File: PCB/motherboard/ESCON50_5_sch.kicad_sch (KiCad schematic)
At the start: 0 parts

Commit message: aggiunto driver escon in libreria e nel progetto schematico
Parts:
- added E1: escon, ESCON:escon_vero, symbol escon50_5:ESCON_50/5
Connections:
- new net +24V: E1.7 (Vcc), E1.8 (Vcc)
- new net +5V: E1.11 (+5_VDC)
- new net GND: E1.10 (GND), E1.23 (GND), E1.9 (GND)
- new net MW1: E1.1 (motor_winding_1), E1.2 (motor_winding_1)
- new net MW2: E1.3 (motor_winding_2), E1.4 (motor_winding_2)
- new net MW3: E1.5 (motor_winding_3), E1.6 (motor_winding_3)

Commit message: test kicad collab
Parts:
- added C14, C16: 150p, Capacitor_SMD:C_1206_3216Metric_Pad1.33x1.80mm_HandSolder, symbol Device:C
- added C15, C17: 330p, Capacitor_SMD:C_1206_3216Metric_Pad1.33x1.80mm_HandSolder, symbol Device:C
- added L2, L3: 22uH, induttorejlpcb_escon:Senza-titolo, symbol PA5433_223NLT:PA5433.223NLT
- added R11, R12: 390, Resistor_SMD:R_1206_3216Metric_Pad1.30x1.75mm_HandSolder, symbol Device:R
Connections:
- net GND: now also C14.2, C16.2, R11.2, R12.2
- net MW2: now also L3.1
- net MW3: now also L2.1
- new net: C15.2, R11.1
- new net: C17.2, R12.1
- new net MW2_motor: C16.1, C17.1, L3.2
- new net MW3_motor: C14.1, C15.1, L2.2
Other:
- moved on the sheet: E1

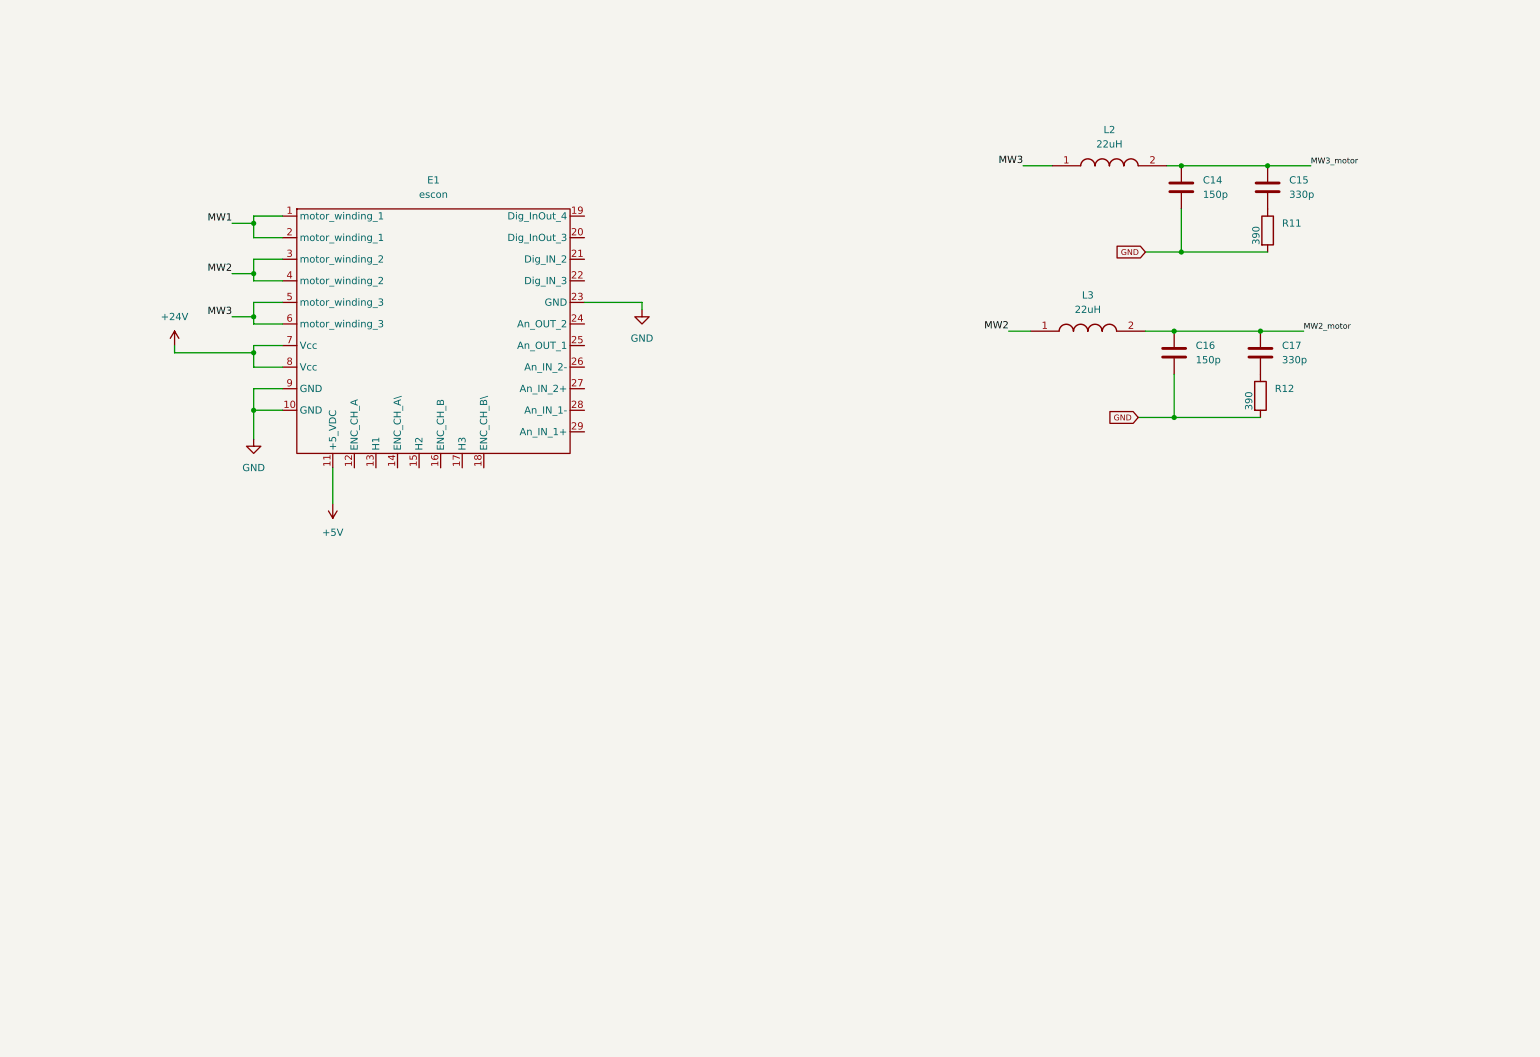
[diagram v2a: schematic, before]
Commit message: added hierrcical labels mcu, added filters for escon + labels
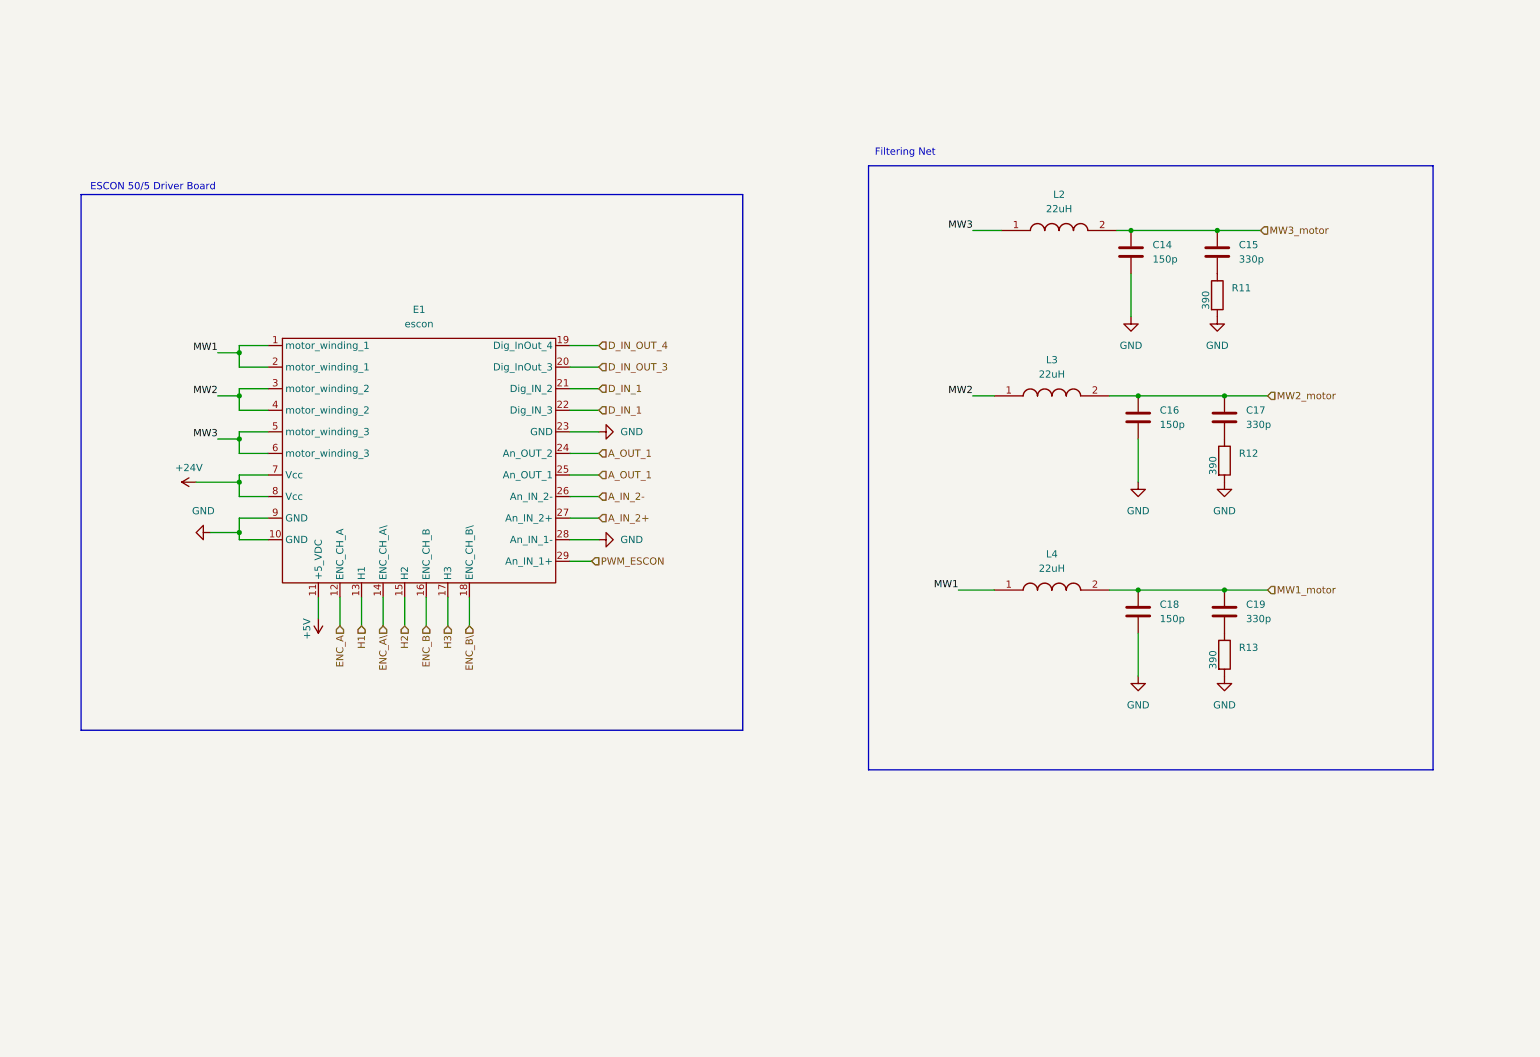
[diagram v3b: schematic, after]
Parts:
- added C18: 150p, Capacitor_SMD:C_1206_3216Metric_Pad1.33x1.80mm_HandSolder, symbol Device:C
- added C19: 330p, Capacitor_SMD:C_1206_3216Metric_Pad1.33x1.80mm_HandSolder, symbol Device:C
- added L4: 22uH, induttorejlpcb_escon:Senza-titolo, symbol PA5433_223NLT:PA5433.223NLT
- added R13: 390, Resistor_SMD:R_1206_3216Metric_Pad1.30x1.75mm_HandSolder, symbol Device:R
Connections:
- net GND: now also E1.28 (An_IN_1-), C18.2, R13.2
- net MW1: now also L4.1
- net ENC_A: now reaches E1.12 (ENC_CH_A)
- net H1: now reaches E1.13 (H1)
- net ENC_A\: now reaches E1.14 (ENC_CH_A\)
- net H2: now reaches E1.15 (H2)
- net ENC_B: now reaches E1.16 (ENC_CH_B)
- net H3: now reaches E1.17 (H3)
- net ENC_B\: now reaches E1.18 (ENC_CH_B\)
- net D_IN_OUT_4: now reaches E1.19 (Dig_InOut_4)
- net D_IN_OUT_3: now reaches E1.20 (Dig_InOut_3)
- net D_IN_1: now reaches E1.21 (Dig_IN_2)
- net D_IN_1: now also E1.22 (Dig_IN_3)
- net A_OUT_1: now reaches E1.24 (An_OUT_2)
- net A_OUT_1: now also E1.25 (An_OUT_1)
- net A_IN_2-: now reaches E1.26 (An_IN_2-)
- net A_IN_2+: now reaches E1.27 (An_IN_2+)
- net PWM_ESCON: now reaches E1.29 (An_IN_1+)
- new net: C19.2, R13.1
- new net MW1_motor: C18.1, C19.1, L4.2
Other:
- note added: "ESCON 50/5 Driver Board"
- note added: "Filtering Net"
- moved on the sheet: C14, C15, C16, C17, E1, L2, L3, R11, R12

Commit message: match label
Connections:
- net A_OUT_1: no longer E1.24 (An_OUT_2)
- new net A_OUT_2: E1.24 (An_OUT_2)
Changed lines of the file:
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@@
 		)
 	)
-	(hierarchical_label "A_OUT_1"
+	(hierarchical_label "A_OUT_2"
 		(shape input)
 		(at 116.84 90.17 0)

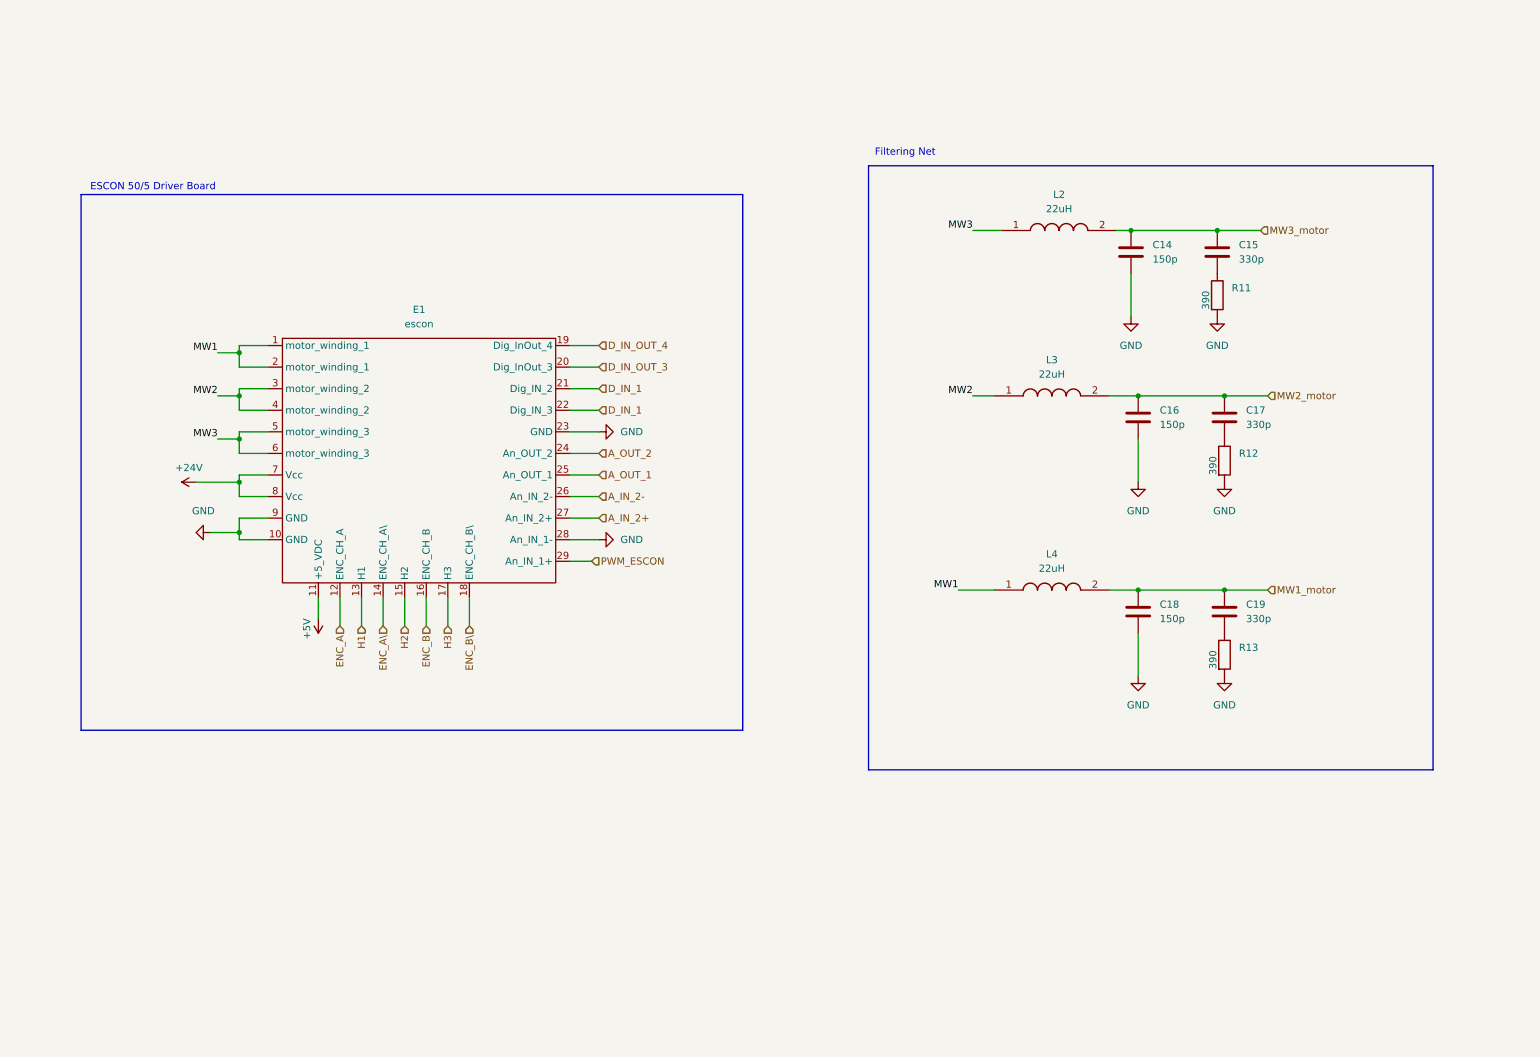
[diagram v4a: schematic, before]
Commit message: reverse current protection on ESCON+others
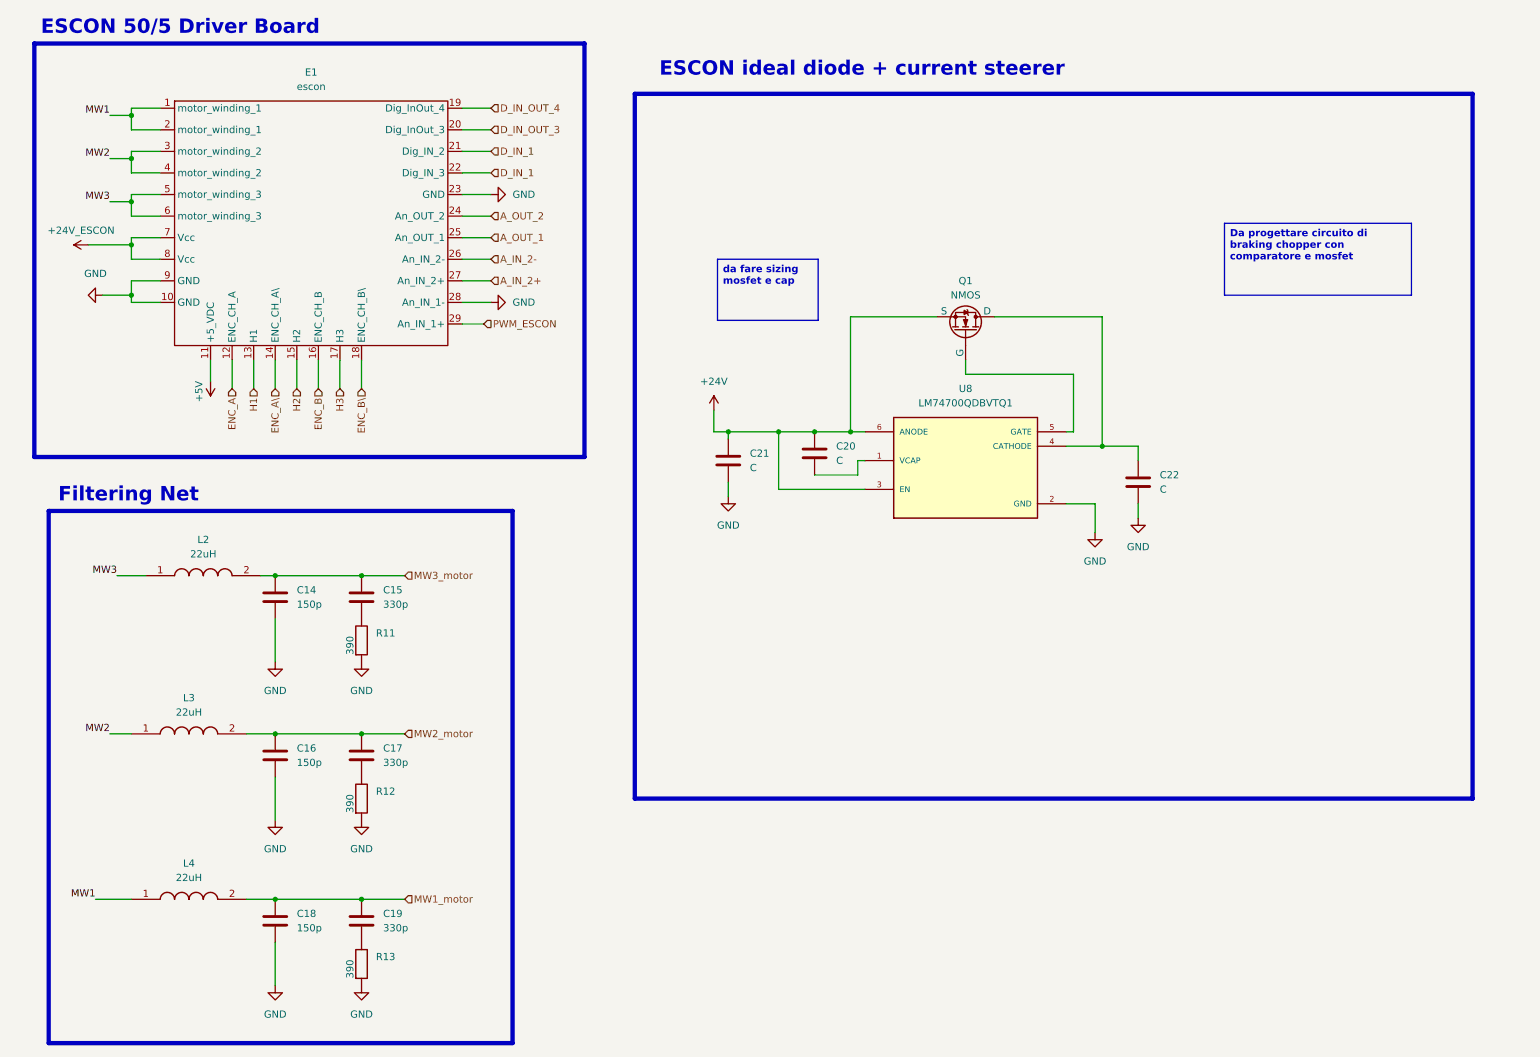
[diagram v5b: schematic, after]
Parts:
- added C20, C21, C22: C, symbol Device:C
- added Q1: NMOS, symbol Simulation_SPICE:NMOS
- added U8: LM74700QDBVTQ1, LM74700QDBVTQ1:SOT95P280X145-6N, symbol LM74700QDBVTQ1:LM74700QDBVTQ1
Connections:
- net +24V: now also C20.1, C21.1, Q1.3 (S), U8.3 (EN), U8.6 (ANODE); no longer E1.7 (Vcc), E1.8 (Vcc)
- net GND: now also C21.2, C22.2, U8.2 (GND)
- new net: C20.2, U8.1 (VCAP)
- new net: C22.1, Q1.1 (D), U8.4 (CATHODE)
- new net: Q1.2 (G), U8.5 (GATE)
- new net +24V_ESCON: E1.7 (Vcc), E1.8 (Vcc)
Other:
- note added: "ESCON ideal diode + current steerer"
- moved on the sheet: C14, C15, C16, C17, C18, C19, E1, L2, L3, L4, R11, R12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

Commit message: collegamenti tra blocchi schematico, sistemati connettori,finita la parte di shunt monitor per back EMF escon, aggiunti status LED, aggiunti bulk cap su alimentazione+altre modifiche
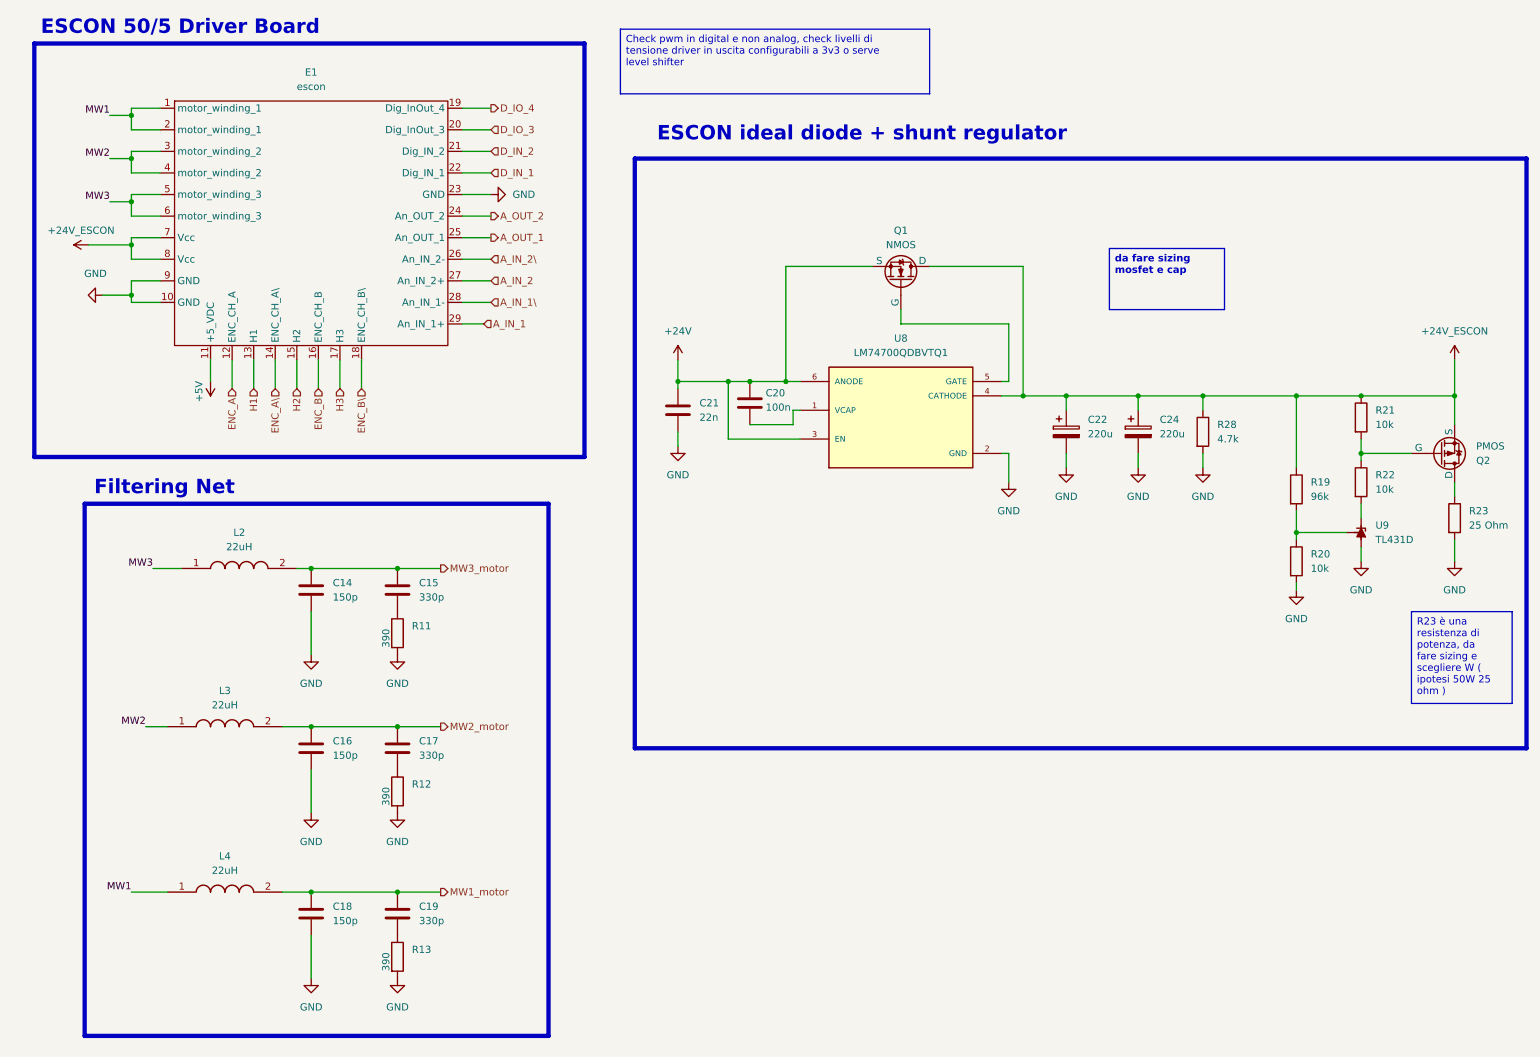
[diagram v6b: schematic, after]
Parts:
- removed C22: C, symbol Device:C
- added C22, C24: 220u, symbol Device:C_Polarized
- added Q2: PMOS, symbol Simulation_SPICE:PMOS
- added R19: 96k, symbol Device:R
- added R20, R21, R22: 10k, symbol Device:R
- added R23: 25 Ohm, symbol Device:R
- added R28: 4.7k, symbol Device:R
- added U9: TL431D, Package_SO:SOIC-8_3.9x4.9mm_P1.27mm, symbol Reference_Voltage:TL431D
- C20: value C -> 100n
- C21: value C -> 22n
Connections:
- net +24V_ESCON: now also Q1.1 (D), U8.4 (CATHODE), C22.1, C24.1, Q2.3 (S), R19.1, R21.1, R28.1
- net D_IN_1: no longer E1.21 (Dig_IN_2)
- net GND: now also C22.2, C24.2, R20.2, R23.2, R28.2, U9.2 (A), U9.3 (A), U9.6 (A), U9.7 (A); no longer E1.28 (An_IN_1-)
- net A_IN_2+ renamed A_IN_2
- net A_IN_2- renamed A_IN_2\
- net D_IN_OUT_3 renamed D_IO_3
- net D_IN_OUT_4 renamed D_IO_4
- net PWM_ESCON renamed A_IN_1
- new net: Q2.1 (D), R23.1
- new net: R22.2, U9.1 (K)
- new net: R19.2, R20.1, U9.8 (REF)
- new net: Q2.2 (G), R21.2, R22.1
- new net A_IN_1\: E1.28 (An_IN_1-)
- new net D_IN_2: E1.21 (Dig_IN_2)
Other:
- note added: "ESCON ideal diode + shunt regulator"
- note removed: "ESCON ideal diode + current steerer"
- moved on the sheet: C14, C15, C16, C17, C18, C19, C20, C21, L2, L3, L4, Q1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

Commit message: schematics need only sizing
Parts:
- C21: footprint (none) -> Capacitor_SMD:C_1206_3216Metric_Pad1.33x1.80mm_HandSolder
- C22: renamed from C20; footprint (none) -> Capacitor_SMD:C_1206_3216Metric_Pad1.33x1.80mm_HandSolder
- C23: renamed from C22; footprint (none) -> Capacitor_SMD:C_Elec_10x10.2
- C24: footprint (none) -> Capacitor_SMD:C_Elec_10x10.2
- E1: footprint ESCON:escon_vero -> escon50_5:escon_vero
- R22: renamed from R28; footprint (none) -> Resistor_SMD:R_1206_3216Metric_Pad1.30x1.75mm_HandSolder
- R23: renamed from R19; footprint (none) -> Resistor_SMD:R_1206_3216Metric_Pad1.30x1.75mm_HandSolder
- R24: renamed from R20; footprint (none) -> Resistor_SMD:R_1206_3216Metric_Pad1.30x1.75mm_HandSolder
- R26: renamed from R21; footprint (none) -> Resistor_SMD:R_1206_3216Metric_Pad1.30x1.75mm_HandSolder
- R27: renamed from R22; footprint (none) -> Resistor_SMD:R_1206_3216Metric_Pad1.30x1.75mm_HandSolder
- renumbered C14 to C15, C18 to C17, C15 to C18, C17 to C19, C19 to C20, L3 to L2, L4 to L3, L2 to L4, R11 to R16, R12 to R17, R13 to R18, R23 to R28, U8 to U6
